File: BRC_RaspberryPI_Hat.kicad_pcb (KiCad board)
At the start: 4 copper layers, 65.5 x 57.2 mm, 23 parts, among them J1 GPIO, U2 SN754410NE, U3 ADS1115IDGS, U4 SN754410NE, U5 SN754410NE

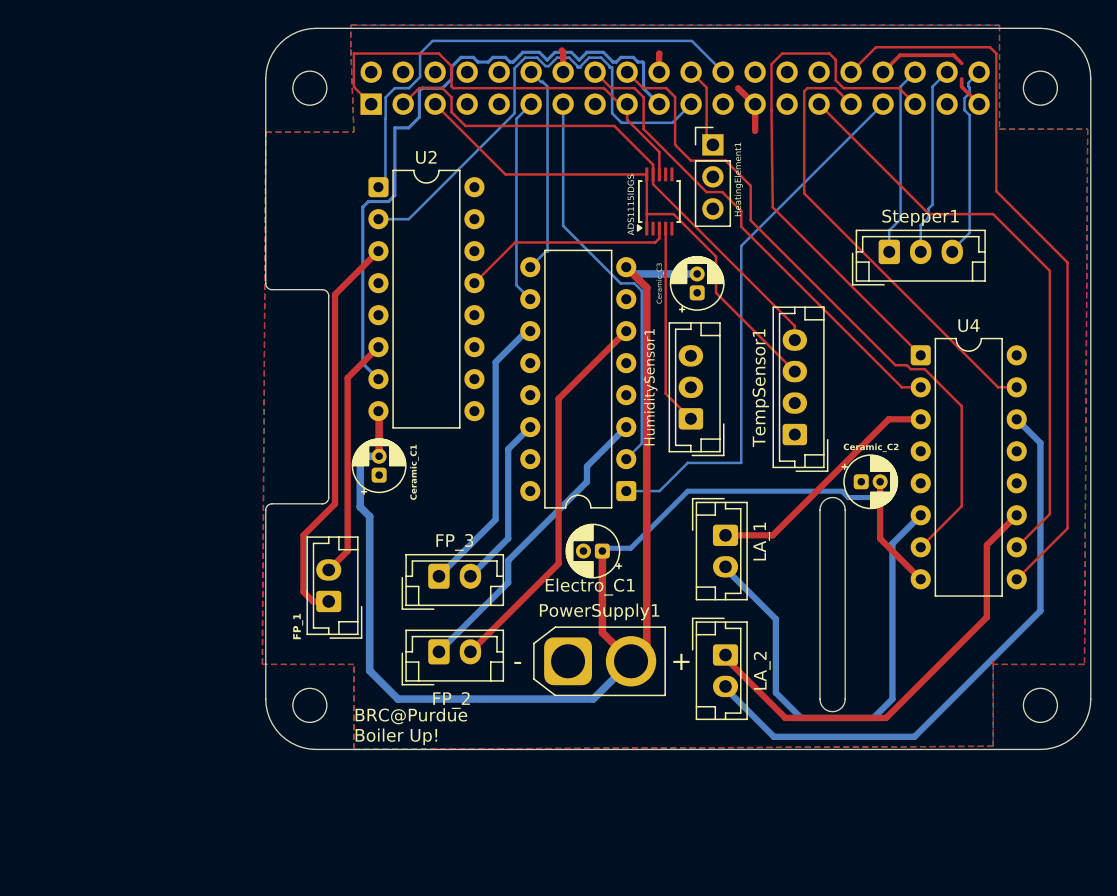
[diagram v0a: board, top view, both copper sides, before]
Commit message: Redesign Raspberry Pi HAT PCB layout
Rework the board as a two-layer layout with updated component placement and routing. Add servo outputs and external servo power, an I2C ID EEPROM, and supporting components; update the project for KiCad 10 and revise design-rule settings.
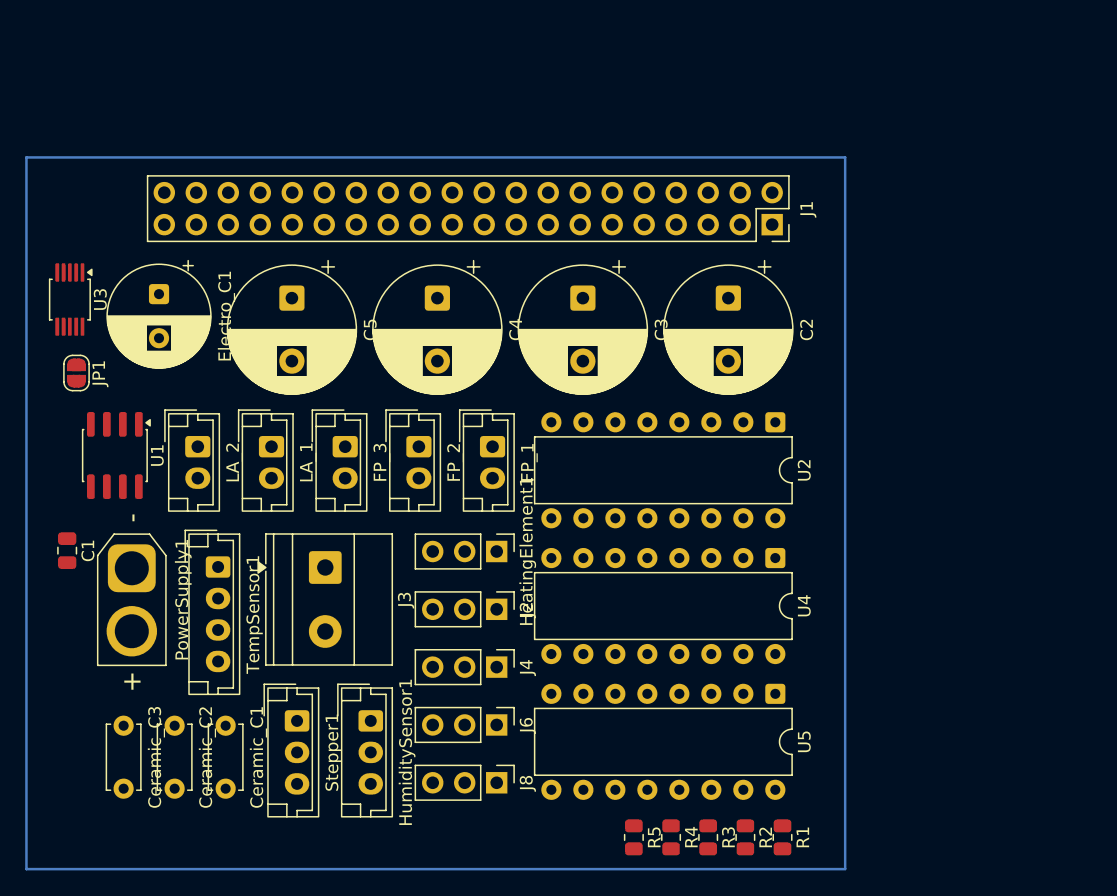
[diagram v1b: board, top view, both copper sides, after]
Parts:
- removed MH1, MH2, MH3, MH4: MountingHole_2.7mm_M2.5, MountingHole:MountingHole_2.7mm_M2.5
- added C1: 100n, Capacitor_SMD:C_0805_2012Metric, F.Cu at (84.2, 84.2)
- added C2: 1000uF/25V, Capacitor_THT:CP_Radial_D10.0mm_P5.00mm, F.Cu at (136.7, 64.2)
- added C3: 1000uF/25V, Capacitor_THT:CP_Radial_D10.0mm_P5.00mm, F.Cu at (125.2, 64.2)
- added C4: 1000uF/25V, Capacitor_THT:CP_Radial_D10.0mm_P5.00mm, F.Cu at (113.6, 64.2)
- added C5: 1000uF/25V, Capacitor_THT:CP_Radial_D10.0mm_P5.00mm, F.Cu at (102.1, 64.2)
- added J2: Servo, Connector_PinHeader_2.54mm:PinHeader_1x03_P2.54mm_Vertical, F.Cu at (118.3, 88.9)
- added J3: ServoPower, TerminalBlock_Phoenix:TerminalBlock_Phoenix_MKDS-1,5-2-5.08_1x02_P5.08mm_Horizontal, F.Cu at (104.7, 85.6)
- added J4: Servo, Connector_PinHeader_2.54mm:PinHeader_1x03_P2.54mm_Vertical, F.Cu at (118.3, 93.5)
- added J6: Servo, Connector_PinHeader_2.54mm:PinHeader_1x03_P2.54mm_Vertical, F.Cu at (118.3, 98.1)
- added J8: Servo, Connector_PinHeader_2.54mm:PinHeader_1x03_P2.54mm_Vertical, F.Cu at (118.3, 102.6)
- added JP1: ID_WP, Jumper:SolderJumper-2_P1.3mm_Open_RoundedPad1.0x1.5mm, F.Cu at (85.0, 70.1)
- added R1: 3.9k, Resistor_SMD:R_0805_2012Metric, F.Cu at (141.0, 107.0)
- added R2: 330, Resistor_SMD:R_0805_2012Metric, F.Cu at (138.1, 107.0)
- added R3: 330, Resistor_SMD:R_0805_2012Metric, F.Cu at (135.1, 107.0)
- added R4: 330, Resistor_SMD:R_0805_2012Metric, F.Cu at (132.2, 107.0)
- added R5: 330, Resistor_SMD:R_0805_2012Metric, F.Cu at (129.2, 107.0)
- added U1: CAT24C256, Package_SO:SOIC-8_3.9x4.9mm_P1.27mm, F.Cu at (88.0, 76.7)
- Ceramic_C1, Ceramic_C2, Ceramic_C3: footprint Capacitor_THT:CP_Radial_D4.0mm_P1.50mm -> Capacitor_THT:C_Disc_D5.0mm_W2.5mm_P5.00mm
- Electro_C1: value 220micro -> 220uF/25V; footprint Capacitor_THT:CP_Radial_D4.0mm_P1.50mm -> Capacitor_THT:CP_Radial_D8.0mm_P3.50mm
- J1: moved to F.Cu
- moved Stepper1 60.0 mm to (102.5, 97.7), turned to -90 degrees
- moved Ceramic_C2 57.8 mm to (92.8, 98.1), turned to -90 degrees
- moved Ceramic_C3 57.0 mm to (88.7, 98.1), turned to -90 degrees
- moved U3 47.4 mm to (84.5, 64.3), turned to -90 degrees
- moved TempSensor1 47.0 mm to (96.2, 85.5), turned to -90 degrees
- moved LA_2 45.0 mm to (94.6, 76.0)
- moved Electro_C1 40.7 mm to (91.5, 63.8), turned to -90 degrees
- moved LA_1 36.7 mm to (100.5, 76.0)
- moved U2 36.6 mm to (140.5, 74.0), turned to -90 degrees
- moved HeatingElement1 36.6 mm to (118.3, 84.3), turned to -90 degrees
- moved PowerSupply1 35.4 mm to (89.4, 85.6), turned to -90 degrees
- moved HumiditySensor1 34.9 mm to (108.3, 97.7), turned to -90 degrees
- moved J1 33.2 mm to (140.2, 58.3)
- moved Ceramic_C1 23.3 mm to (96.8, 98.1), turned to -90 degrees
- moved U5 20.0 mm to (140.5, 95.6), turned to -90 degrees
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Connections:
- net GPIO7/SPI0.CE1 renamed /GPIO7/SPI0.CE1
- net Net-(PowerSupply1-Pin_2) renamed /+12V
- J1 pad 37: unconnected-(J1-Pin_37-Pad37) -> GPIO26
- U3 pad 1: /GPIO3/SCL1 -> /GPIO2/SDA1
- U5 pad 15: unconnected-(U5-4A-Pad15) -> GND
- U5 pad 7: unconnected-(U5-2A-Pad7) -> GND
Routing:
- net /+12V: track 128.7 -> 0.00 mm
- net /GPIO12/PWM0: track 58.3 -> 0.00 mm
- net /GPIO24: track 53.9 -> 0.00 mm
- net GPIO10/SPI0.MOSI: track 52.6 -> 0.00 mm
- net Net-(LA_2-Pin_2): track 46.9 -> 0.00 mm
- net /GPIO5: track 46.8 -> 0.00 mm
- net /GPIO13/PWM1: track 43.2 -> 0.00 mm
- net /GPIO19/PCM.FS: track 42.3 -> 0.00 mm
- net /GPIO2/SDA1: track 42.2 -> 0.00 mm
- net /GPIO3/SCL1: track 42.0 -> 0.00 mm
- net GPIO9/SPI0.MISO: track 38.5 -> 0.00 mm
- net /GPIO23: track 38.4 -> 0.00 mm
- net GPIO8: track 38.1 -> 0.00 mm
- net Net-(LA_1-Pin_2): track 37.9 -> 0.00 mm
- net Net-(J1-Pin_31): track 35.7 -> 0.00 mm
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- removed copper zone on B.Cu, net +5V
- removed copper zone on F.Cu, net GND
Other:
- board outline removed
- copper layers 4 -> 2
- board text removed: "BRC@Purdue Boiler Up!"
- board text removed: "CAMERA (OPTIONAL)"
- board text removed: "DISPLAY (OPTIONAL)"
- board text removed: "PoE"
- board text removed: "RJ45"
- board text removed: "USB"
